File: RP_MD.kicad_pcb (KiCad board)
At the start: 2 copper layers, 73.8 x 50 mm, 105 parts, among them CN1 XT30PW-M, CN2 XT30PW, CN3 XT30PW, J1 USB_C_Receptacle, J2 Conn_01x04_Female, J3 Conn_01x04_Female, J4 Conn_01x06_Female, J5 Conn_01x06_Female, J6 Conn_01x04_Female, J7 Conn_01x03_Male, J8 Conn_01x03_Female, Q1 TPN1R603PL, Q2 TPN1R603PL, Q3 TPN1R603PL, Q4 TPN1R603PL, Q5 TPN1R603PL, Q6 TPN1R603PL, Q7 TPN1R603PL, Q8 TPN1R603PL, SW1 SW_Push, SW2 SW_Push, SW3 SW_Push, SW4 SW_Push, U1 DGD0506A, U10 NJM78L005, U2 MCP6C02T, U3 DGD0506A, U4 W25Q16JV, U5 RP2040, U6 DGD0506A, U7 MCP6C02T, U8 DGD0506A, U9 MAX3458ED, Y1 445I23D12M00000

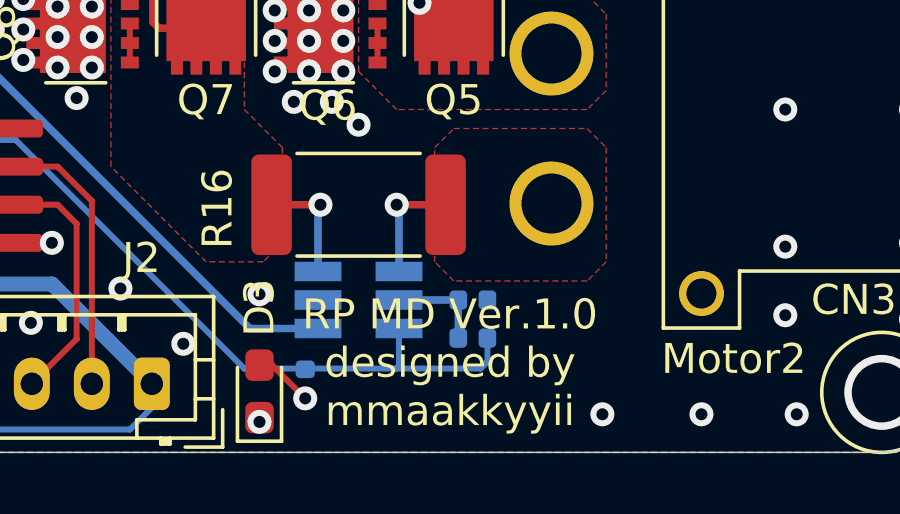
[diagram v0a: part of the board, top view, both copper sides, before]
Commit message: add debug pin and fix AVDD
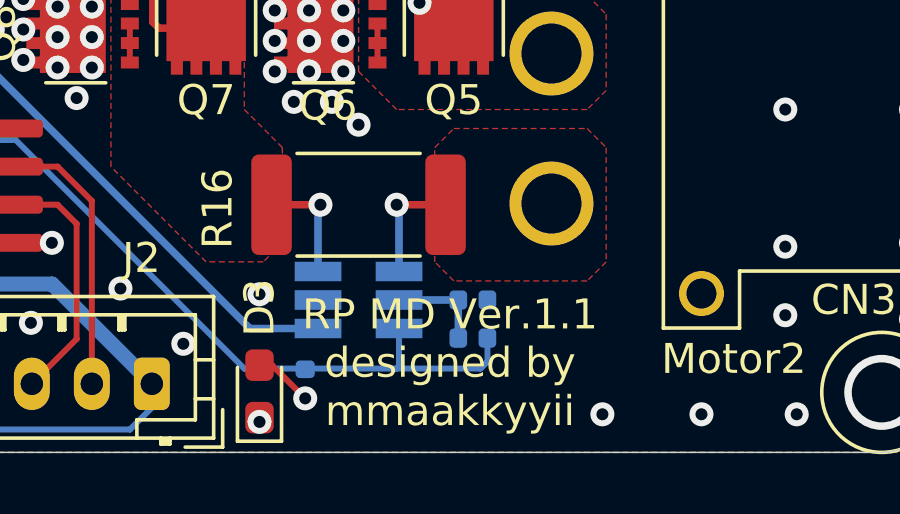
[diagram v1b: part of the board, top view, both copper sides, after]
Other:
- board text added: "RP MD Ver.1.1 designed by mmaakkyyii"
- board text removed: "RP MD Ver.1.0 designed by mmaakkyyii"
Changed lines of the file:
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@@
   )
   (setup
-    (last_trace_width 0.2)
+    (last_trace_width 0.25)
     (user_trace_width 0.2)
     (user_trace_width 0.5)
@@
     (arrow2b (pts (xy 167.22 100.33) (xy 166.633579 99.203496)))
   )
-  (gr_text "RP MD Ver.1.0\ndesigned by \nmmaakkyyii" (at 147.828 97.3455) (layer F.SilkS)
+  (gr_text "RP MD Ver.1.1\ndesigned by \nmmaakkyyii" (at 147.828 97.3455) (layer F.SilkS)
     (effects (font (size 1 1) (thickness 0.15)))
   )
@@
   (via (at 111.22 98.33) (size 2.5) (drill 2) (layers F.Cu B.Cu) (net 0))
   (via (at 111.22 52.33) (size 2.5) (drill 2) (layers F.Cu B.Cu) (net 0))
-  (via (at 160.782 60.96) (size 0.8) (drill 0.4) (layers F.Cu B.Cu) (net 2))
-  (via (at 162.052 60.96) (size 0.8) (drill 0.4) (layers F.Cu B.Cu) (net 2))
-  (via (at 163.322 60.96) (size 0.8) (drill 0.4) (layers F.Cu B.Cu) (net 2))
-  (via (at 143.129 87.63) (size 0.8) (drill 0.4) (layers F.Cu B.Cu) (net 2))
-  (via (at 144.272 87.63) (size 0.8) (drill 0.4) (layers F.Cu B.Cu) (net 2))
-  (via (at 141.986 86.614) (size 0.8) (drill 0.4) (layers F.Cu B.Cu) (net 2))
-  (via (at 143.129 86.614) (size 0.8) (drill 0.4) (layers F.Cu B.Cu) (net 2))
-  (via (at 144.272 86.614) (size 0.8) (drill 0.4) (layers F.Cu B.Cu) (net 2))
-  (via (at 144.272 85.598) (size 0.8) (drill 0.4) (layers F.Cu B.Cu) (net 2))
-  (via (at 141.986 85.598) (size 0.8) (drill 0.4) (layers F.Cu B.Cu) (net 2))
-  (via (at 143.129 85.598) (size 0.8) (drill 0.4) (layers F.Cu B.Cu) (net 2))
-  (via (at 141.986 87.63) (size 0.8) (drill 0.4) (layers F.Cu B.Cu) (net 2))
-  (via (at 134.747 87.503) (size 0.8) (drill 0.4) (layers F.Cu B.Cu) (net 2))
-  (via (at 135.89 87.503) (size 0.8) (drill 0.4) (layers F.Cu B.Cu) (net 2))
-  (via (at 134.747 86.487) (size 0.8) (drill 0.4) (layers F.Cu B.Cu) (net 2))
-  (via (at 135.89 86.487) (size 0.8) (drill 0.4) (layers F.Cu B.Cu) (net 2))
-  (via (at 135.89 85.471) (size 0.8) (drill 0.4) (layers F.Cu B.Cu) (net 2))
-  (via (at 134.747 85.471) (size 0.8) (drill 0.4) (layers F.Cu B.Cu) (net 2))
-  (via (at 134.62 69.977) (size 0.8) (drill 0.4) (layers F.Cu B.Cu) (net 2))
-  (via (at 134.62 68.834) (size 0.8) (drill 0.4) (layers F.Cu B.Cu) (net 2))
-  (via (at 134.62 70.993) (size 0.8) (drill 0.4) (layers F.Cu B.Cu) (net 2))
-  (via (at 135.763 70.993) (size 0.8) (drill 0.4) (layers F.Cu B.Cu) (net 2))
-  (via (at 135.763 69.977) (size 0.8) (drill 0.4) (layers F.Cu B.Cu) (net 2))
-  (via (at 135.763 68.834) (size 0.8) (drill 0.4) (layers F.Cu B.Cu) (net 2))
-  (via (at 144.399 70.231) (size 0.8) (drill 0.4) (layers F.Cu B.Cu) (net 2))
-  (via (at 144.399 69.215) (size 0.8) (drill 0.4) (layers F.Cu B.Cu) (net 2))
-  (via (at 143.256 70.231) (size 0.8) (drill 0.4) (layers F.Cu B.Cu) (net 2))
-  (via (at 143.256 69.215) (size 0.8) (drill 0.4) (layers F.Cu B.Cu) (net 2))
   (segment (start 123.881 74.792) (end 123.881 75.4295) (width 0.2) (layer F.Cu) (net 1))
   (segment (start 123.881 74.399) (end 123.881 74.792) (width 0.2) (layer F.Cu) (net 1))
@@
   (segment (start 146.558 80.772) (end 146.05 80.772) (width 0.2) (layer B.Cu) (net 1))
   (segment (start 146.05 80.772) (end 139.7 80.772) (width 0.2) (layer B.Cu) (net 1))
+  (via (at 160.782 60.96) (size 0.8) (drill 0.4) (layers F.Cu B.Cu) (net 2))
+  (via (at 162.052 60.96) (size 0.8) (drill 0.4) (layers F.Cu B.Cu) (net 2))
+  (via (at 163.322 60.96) (size 0.8) (drill 0.4) (layers F.Cu B.Cu) (net 2))
+  (via (at 143.129 87.63) (size 0.8) (drill 0.4) (layers F.Cu B.Cu) (net 2))
+  (via (at 144.272 87.63) (size 0.8) (drill 0.4) (layers F.Cu B.Cu) (net 2))
+  (via (at 141.986 86.614) (size 0.8) (drill 0.4) (layers F.Cu B.Cu) (net 2))
+  (via (at 143.129 86.614) (size 0.8) (drill 0.4) (layers F.Cu B.Cu) (net 2))
+  (via (at 144.272 86.614) (size 0.8) (drill 0.4) (layers F.Cu B.Cu) (net 2))
+  (via (at 144.272 85.598) (size 0.8) (drill 0.4) (layers F.Cu B.Cu) (net 2))
+  (via (at 141.986 85.598) (size 0.8) (drill 0.4) (layers F.Cu B.Cu) (net 2))
+  (via (at 143.129 85.598) (size 0.8) (drill 0.4) (layers F.Cu B.Cu) (net 2))
+  (via (at 141.986 87.63) (size 0.8) (drill 0.4) (layers F.Cu B.Cu) (net 2))
+  (via (at 134.747 87.503) (size 0.8) (drill 0.4) (layers F.Cu B.Cu) (net 2))
+  (via (at 135.89 87.503) (size 0.8) (drill 0.4) (layers F.Cu B.Cu) (net 2))
+  (via (at 134.747 86.487) (size 0.8) (drill 0.4) (layers F.Cu B.Cu) (net 2))
+  (via (at 135.89 86.487) (size 0.8) (drill 0.4) (layers F.Cu B.Cu) (net 2))
+  (via (at 135.89 85.471) (size 0.8) (drill 0.4) (layers F.Cu B.Cu) (net 2))
+  (via (at 134.747 85.471) (size 0.8) (drill 0.4) (layers F.Cu B.Cu) (net 2))
+  (via (at 134.62 69.977) (size 0.8) (drill 0.4) (layers F.Cu B.Cu) (net 2))
+  (via (at 134.62 68.834) (size 0.8) (drill 0.4) (layers F.Cu B.Cu) (net 2))
+  (via (at 134.62 70.993) (size 0.8) (drill 0.4) (layers F.Cu B.Cu) (net 2))
+  (via (at 135.763 70.993) (size 0.8) (drill 0.4) (layers F.Cu B.Cu) (net 2))
+  (via (at 135.763 69.977) (size 0.8) (drill 0.4) (layers F.Cu B.Cu) (net 2))
+  (via (at 135.763 68.834) (size 0.8) (drill 0.4) (layers F.Cu B.Cu) (net 2))
+  (via (at 144.399 70.231) (size 0.8) (drill 0.4) (layers F.Cu B.Cu) (net 2))
+  (via (at 144.399 69.215) (size 0.8) (drill 0.4) (layers F.Cu B.Cu) (net 2))
+  (via (at 143.256 70.231) (size 0.8) (drill 0.4) (layers F.Cu B.Cu) (net 2))
+  (via (at 143.256 69.215) (size 0.8) (drill 0.4) (layers F.Cu B.Cu) (net 2))
   (via (at 127.127 98.044) (size 0.8) (drill 0.4) (layers F.Cu B.Cu) (net 2))
   (via (at 128.27 98.044) (size 0.8) (drill 0.4) (layers F.Cu B.Cu) (net 2))

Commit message: v1.1
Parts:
- removed R24, R25: 10k, Resistor_SMD:R_0402_1005Metric
- added C27: 0.1u 50V, Capacitor_SMD:C_0402_1005Metric, B.Cu at (145.3, 81.5)
- added C28: 0.1u 50V, Capacitor_SMD:C_0402_1005Metric, B.Cu at (145.5, 98.0)
- added J9: Conn_01x03_Female, Connector_JST:JST_PH_B3B-PH-SM4-TB_1x03-1MP_P2.00mm_Vertical, B.Cu at (119.6, 95.8)
- added R43: 51k, Resistor_SMD:R_0402_1005Metric, F.Cu at (99.3, 67.8)
- added R44: 51k, Resistor_SMD:R_0402_1005Metric, F.Cu at (93.7, 67.8)
- R40: value R -> 100k
- R41: value R -> 15k
- moved SW3 9.43 mm to (111.3, 57.4)
- moved J7 5.91 mm to (111.0, 62.7)
- moved U9 4.77 mm to (128.8, 87.1), turned to 270 degrees
- moved R41 2.22 mm to (132.8, 74.9), turned to 0 degrees
- moved C12 1.41 mm to (122.9, 85.9)
- moved C13 1.41 mm to (124.0, 85.9)
- moved C26 0.40 mm to (124.7, 93.7)
- moved U10 0.30 mm to (128.0, 95.7)
- moved J2 0.25 mm to (137.9, 98.3)
- moved R30 0.13 mm to (117.9, 58.2)
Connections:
- net Net-(J1-PadA1) renamed GNDA
- J1 pad A5: (no net) -> Net-(J1-PadA5)
- J1 pad B5: (no net) -> Net-(J1-PadB5)
- U5 pad 24: (no net) -> /Sheet625A1F16/SWCLK
- U5 pad 25: (no net) -> /Sheet625A1F16/SWDIO
- U5 pad 43: (no net) -> +3V3
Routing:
- net /Sheet625A1F16/SWDIO: track 0.00 -> 20.0 mm, vias 0 -> 1
- net /Sheet625A1F16/SWCLK: track 0.00 -> 18.3 mm, vias 0 -> 1
- net /DI: track 13.9 -> 4.77 mm
- net Net-(J1-PadB5): track 0.00 -> 7.38 mm, vias 0 -> 2
- net Net-(R8-Pad2): track 8.03 -> 15.3 mm
- net +3V3: track 207.6 -> 214.3 mm
- net /DE_~RE: track 16.9 -> 10.6 mm
- net Net-(J2-Pad3): track 8.16 -> 13.2 mm
- net Net-(J2-Pad2): track 9.02 -> 13.4 mm
- net /Sheet625A1F16/SW2: track 26.5 -> 22.8 mm, vias 1 -> 0
- net +5V: track 93.4 -> 97.0 mm
- net /Vshunt2: track 31.3 -> 34.1 mm
- net Net-(J1-PadA5): track 0.00 -> 2.67 mm
- net /Sheet625A1F16/USB_DP: track 25.9 -> 28.4 mm
- net /Sheet625A1F16/SW1: track 23.0 -> 20.7 mm, vias 1 -> 0
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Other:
- outline, holes or cut-outs redrawn
- board text added: "RS485"

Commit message: kicad6 v1.2
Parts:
- removed J1: USB_C_Receptacle, Connector_USB:USB_C_Receptacle_Amphenol_12401610E4-2A
- removed J8: Conn_01x03_Female, Connector_PinHeader_2.54mm:PinHeader_1x03_P2.54mm_Horizontal
- removed R43, R44: 51k, Resistor_SMD:R_0402_1005Metric
- moved Q4 2.21 mm to (138.4, 70.6), turned to -90 degrees
- moved Q8 2.17 mm to (138.4, 87.0), turned to -90 degrees
- moved Q7 1.76 mm to (140.6, 83.6), turned to 0 degrees
- moved Q3 1.55 mm to (140.6, 67.3), turned to 0 degrees
- moved Q5 1.53 mm to (147.8, 83.6), turned to 0 degrees
- moved Q1 1.28 mm to (147.8, 67.3), turned to 0 degrees
- moved Q6 1.13 mm to (145.5, 87.0), turned to -90 degrees
- moved Q2 1.08 mm to (145.5, 70.6), turned to -90 degrees
- moved R6 1.02 mm to (136.1, 68.2)
- moved R18 0.81 mm to (136.1, 84.5)
- moved R2 0.13 mm to (143.5, 66.4)
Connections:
- net +3V3 renamed +3.3V
- net /DE_~RE renamed /DE_~{RE}
- Q1 pad 1: VCC -> Net-(C2-Pad1)
- Q1 pad 3: Net-(C2-Pad1) -> VCC
- Q2 pad 1: Net-(C2-Pad1) -> GND
- Q2 pad 3: GND -> Net-(C2-Pad1)
- Q3 pad 1: VCC -> Net-(C4-Pad1)
- Q3 pad 3: Net-(C4-Pad1) -> VCC
- Q4 pad 1: Net-(C4-Pad1) -> GND
- Q4 pad 3: GND -> Net-(C4-Pad1)
- Q5 pad 1: VCC -> Net-(C21-Pad1)
- Q5 pad 3: Net-(C21-Pad1) -> VCC
- Q6 pad 1: Net-(C21-Pad1) -> GND
- Q6 pad 3: GND -> Net-(C21-Pad1)
- Q7 pad 1: VCC -> Net-(C23-Pad1)
- Q7 pad 3: Net-(C23-Pad1) -> VCC
- Q8 pad 1: Net-(C23-Pad1) -> GND
- Q8 pad 3: GND -> Net-(C23-Pad1)
- U1 pad 5: (no net) -> unconnected-(U1-Pad5)
- U3 pad 5: (no net) -> unconnected-(U3-Pad5)
- U6 pad 5: (no net) -> unconnected-(U6-Pad5)
- U8 pad 5: (no net) -> unconnected-(U8-Pad5)
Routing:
- net /Sheet625A1F16/_USB_DM: track 11.1 -> 0.00 mm, vias 2 -> 0
- net Net-(J1-PadA4): track 10.2 -> 0.00 mm
- net VCC: track 46.6 -> 39.0 mm
- net Net-(J1-PadB5): track 7.38 -> 0.00 mm, vias 2 -> 0
- net GNDA: track 6.54 -> 0.00 mm
- net /Sheet625A1F16/_USB_DP: track 6.35 -> 0.00 mm
- net Net-(R18-Pad1): track 1.57 -> 5.05 mm
- net Net-(R6-Pad1): track 1.57 -> 5.02 mm
- net Net-(R5-Pad1): track 1.99 -> 5.32 mm
- net Net-(R3-Pad1): track 2.39 -> 5.55 mm
- net Net-(R15-Pad1): track 2.12 -> 5.28 mm
- net Net-(R17-Pad1): track 1.99 -> 4.86 mm
- net Net-(J1-PadA5): track 2.67 -> 0.00 mm
- net Net-(C21-Pad1): track 15.6 -> 12.9 mm
- net Net-(C23-Pad1): track 15.9 -> 13.4 mm
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- removed copper zone on F.Cu, net GNDA
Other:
- board size 73.8 x 50 mm -> 55 x 50 mm
- net class Default removed
- board text added: "RP MD Ver.1.2 designed by mmaakkyyii"
- board text added: "Vin~24V 30A"
- board text removed: "RP MD Ver.1.1 designed by mmaakkyyii"
- board text removed: "Vin~~25V"
